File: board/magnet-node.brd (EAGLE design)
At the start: 22.8 x 23.1 mm, 28 parts, among them X1 SMA-142-0701-801/806

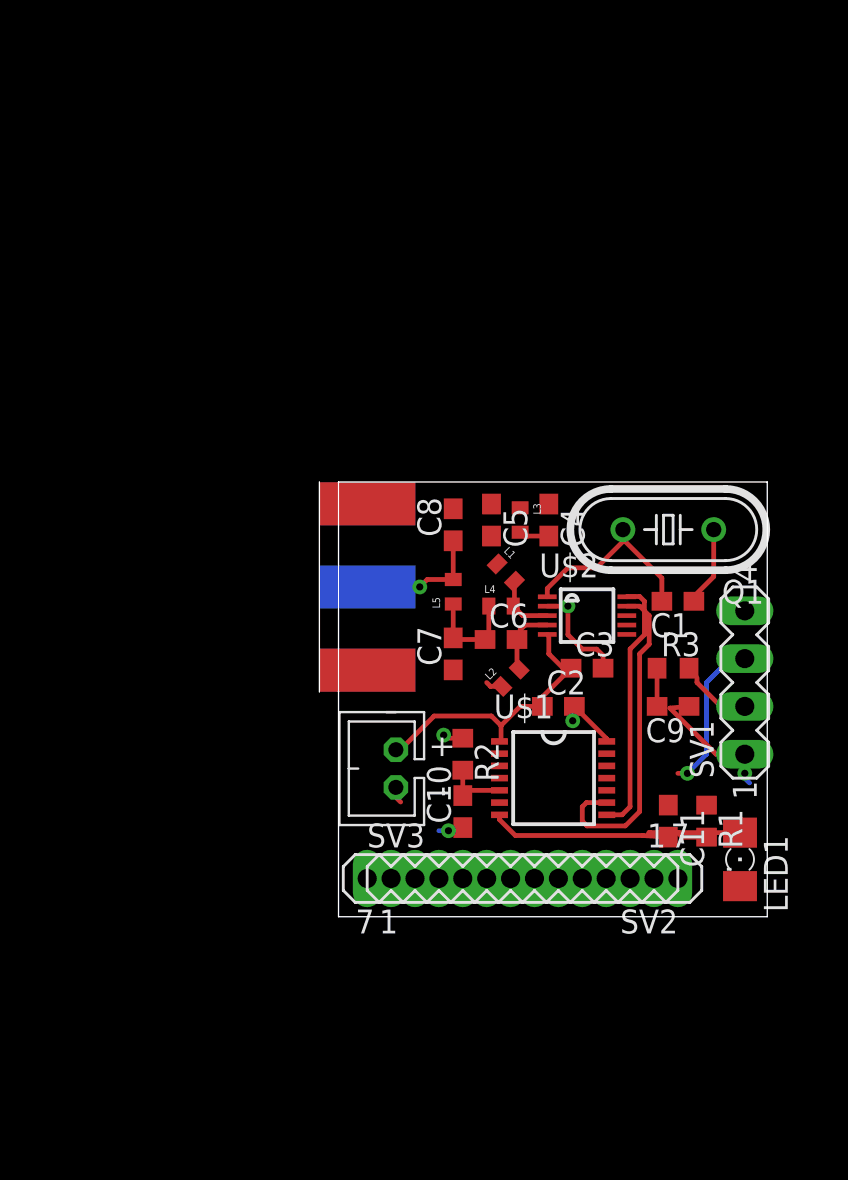
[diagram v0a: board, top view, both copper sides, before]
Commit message: initial route
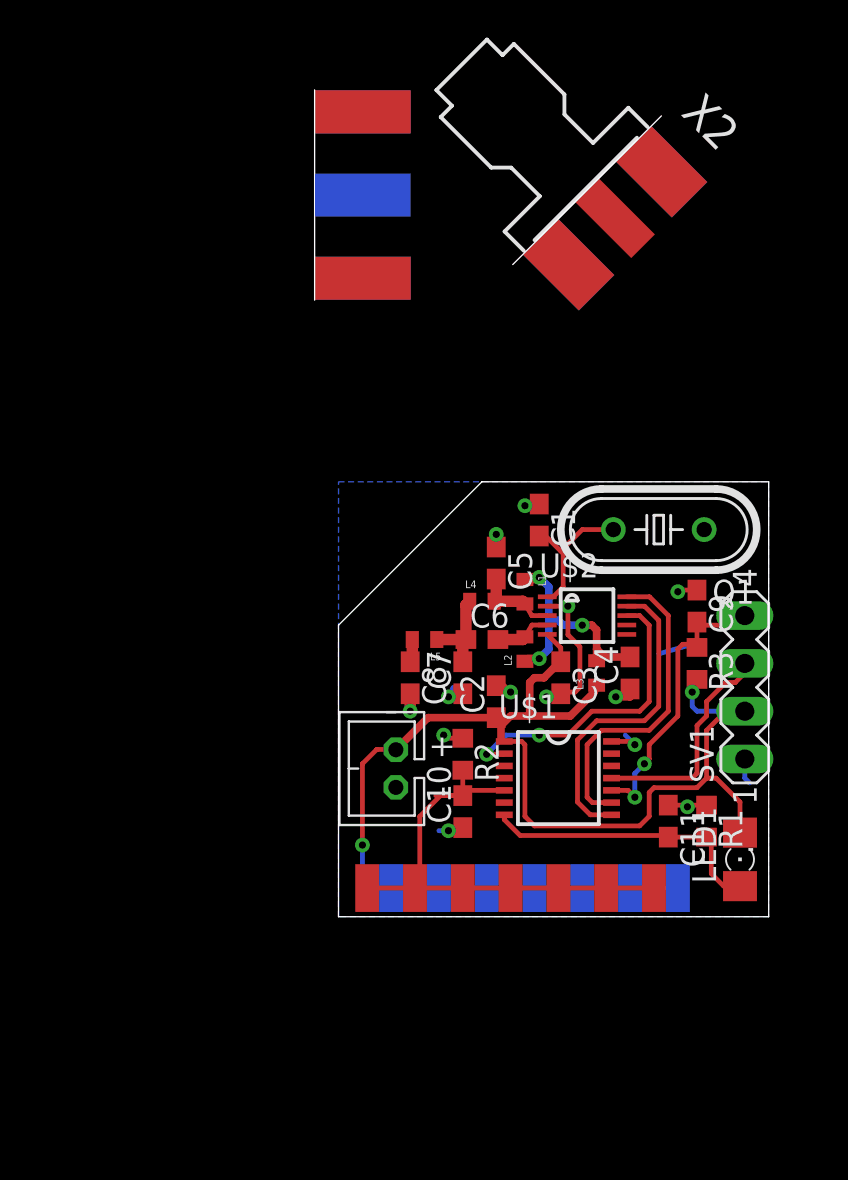
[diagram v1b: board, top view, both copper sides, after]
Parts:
- added X2: SMA-142-0711-821/826, con-coax:J502-ND-142-0711-821/826
- SV2, SV3: device con-lstb:MA07-1 -> Mine:MA07-1-SMD
- moved X1 20.8 mm to (-1.27, 42.9)
- moved C4 9.20 mm to (15.5, 17.5), turned to 90 degrees
- moved L3 9.09 mm to (13.7, 17.5), turned to 90 degrees
- moved C1 8.54 mm to (10.7, 25.7), turned to 270 degrees
- moved C8 8.44 mm to (3.81, 17.3), turned to 270 degrees
- moved C9 5.48 mm to (19.1, 21.1), turned to 270 degrees
- moved C2 3.31 mm to (8.38, 16.0), turned to 90 degrees
- moved L5 2.96 mm to (4.57, 19.3), turned to 180 degrees
- moved C5 2.30 mm to (8.38, 23.4)
- moved L2 1.70 mm to (9.91, 18.8), turned to 90 degrees
- moved C3 1.49 mm to (11.8, 17.3), turned to 270 degrees
- moved L1 1.44 mm to (9.91, 21.8), turned to 270 degrees
- moved C7 1.37 mm to (6.60, 17.3)
- moved SV2 1.37 mm to (10.4, 6.10), flipped to the bottom, turned to 0 degrees
- moved SV3 1.37 mm to (9.14, 6.10)
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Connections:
- new net N$1: U$1.2, U$2.8
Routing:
- net +3V3: track 18.6 -> 75.3 mm, vias 0 -> 2
- net N$12: track 3.41 -> 27.2 mm
- net N$1: track 0.00 -> 16.2 mm, vias 0 -> 2
- net N$15: track 2.03 -> 15.8 mm, vias 0 -> 2
- net N$4: track 2.50 -> 12.7 mm, vias 0 -> 3
- net N$10: track 6.77 -> 1.23 mm, vias 1 -> 0
- net N$3: track 13.2 -> 17.0 mm
- net N$2: track 8.31 -> 11.8 mm, vias 1 -> 0
- net N$5: track 10.3 -> 7.76 mm
- net N$13: track 17.1 -> 15.2 mm
- net N$8: track 3.36 -> 4.75 mm
- net N$6: track 18.2 -> 17.0 mm
- net N$9: track 3.75 -> 3.05 mm
- net GND: vias 5 -> 13
- added copper zone on layer 16, net GND
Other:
- board size 22.8 x 23.1 mm -> 22.9 x 23.1 mm

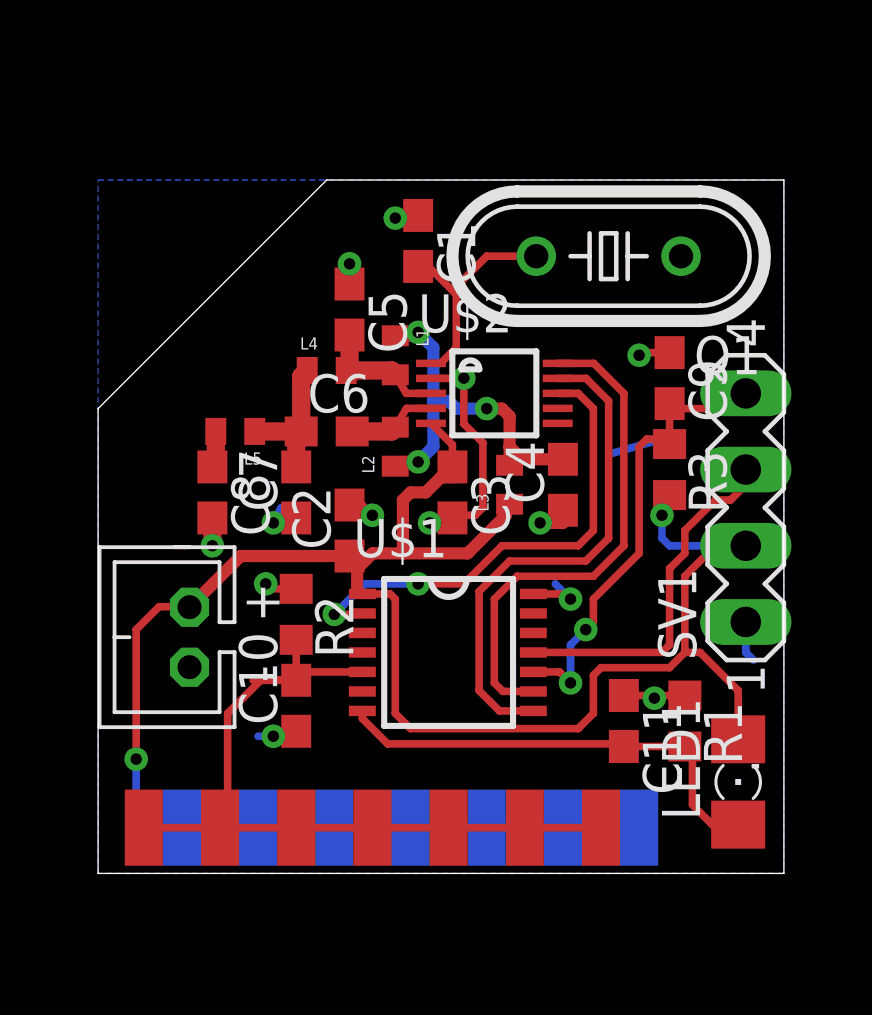
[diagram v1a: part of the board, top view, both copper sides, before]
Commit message: changing sensor power arragment
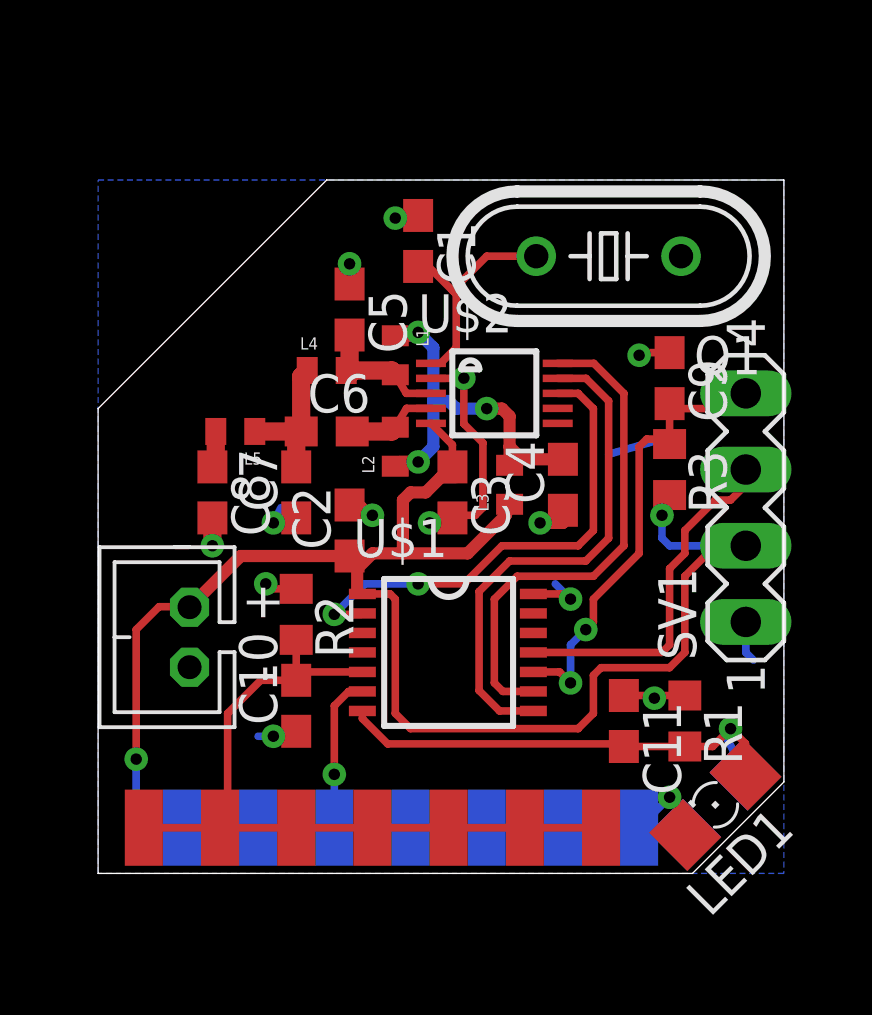
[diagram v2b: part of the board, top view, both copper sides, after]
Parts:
- added LED2: (no value), led:1206
- moved LED1 1.08 mm to (20.6, 6.86), turned to 225 degrees
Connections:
- new net VCCS: LED1.C, LED2.C, SV2.1, SV2.2, SV2.3, SV2.4, SV2.5, SV2.6, SV2.7, U$1.6
- net +3V3: no longer LED1.C, SV2.1, SV2.2, SV2.3, SV2.4, SV2.5, SV2.6, SV2.7
- net N$13: now also LED2.A
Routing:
- net VCCS: track 0.00 -> 26.1 mm, vias 0 -> 2
- net +3V3: track 75.3 -> 55.1 mm
- net N$13: track 15.2 -> 17.3 mm, vias 0 -> 1
- net N$12: track 27.2 -> 25.7 mm
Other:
- outline, holes or cut-outs redrawn
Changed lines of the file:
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@@
 <board>
 <plain>
-<wire x1="0" y1="4.572" x2="22.86" y2="4.572" width="0" layer="20"/>
+<wire x1="0" y1="4.572" x2="19.812" y2="4.572" width="0" layer="20"/>
 <dimension x1="0" y1="4.572" x2="0" y2="27.676" x3="-13.208" y3="16.124" textsize="1.778" layer="51"/>
 <dimension x1="0" y1="27.676" x2="22.784" y2="27.676" x3="11.392" y3="34.036" textsize="1.778" layer="51"/>
 <wire x1="7.62" y1="27.686" x2="0" y2="20.066" width="0" layer="20"/>
 <wire x1="7.62" y1="27.686" x2="22.86" y2="27.686" width="0" layer="20"/>
-<wire x1="22.86" y1="27.686" x2="22.86" y2="4.572" width="0" layer="20"/>
+<wire x1="22.86" y1="27.686" x2="22.86" y2="7.62" width="0" layer="20"/>
 <wire x1="0" y1="20.066" x2="0" y2="4.572" width="0" layer="20"/>
+<wire x1="19.812" y1="4.572" x2="22.86" y2="7.62" width="0" layer="20"/>
 </plain>
 <attributes>
@@
 <element name="R1" library="rcl" package="R0603" value="" x="19.558" y="9.652" rot="R270"/>
 <element name="R2" library="rcl" package="R0603" value="" x="6.604" y="13.208" rot="R270"/>
-<element name="LED1" library="led" package="1206" value="" x="21.336" y="7.62" rot="R90"/>
+<element name="LED1" library="led" package="1206" value="" x="20.574" y="6.858" rot="R225"/>
 <element name="R3" library="rcl" package="R0603" value="" x="19.05" y="18.034" rot="R270"/>
 <element name="C9" library="rcl" package="C0603" value="" x="19.05" y="21.082" rot="R270"/>
@@
 <attribute name="OC_FARNELL" value="1019328" x="13.208" y="43.18" size="1.778" layer="27" rot="R315" display="off"/>
 </element>
+<element name="LED2" library="led" package="1206" value="" x="20.574" y="6.858" rot="MR315"/>
 </elements>
 <signals>
@@
 <contactref element="J2" pad="1"/>
 <contactref element="L3" pad="1"/>
-<contactref element="LED1" pad="C"/>
-<contactref element="SV2" pad="7"/>
-<contactref element="SV2" pad="6"/>
-<contactref element="SV2" pad="5"/>
-<contactref element="SV2" pad="4"/>
-<contactref element="SV2" pad="3"/>
-<contactref element="SV2" pad="2"/>
-<contactref element="SV2" pad="1"/>
 <contactref element="R3" pad="2"/>
 <wire x1="3.048" y1="13.446" x2="3.286" y2="13.446" width="0.254" layer="1"/>
@@
 <wire x1="10.414" y1="9.398" x2="9.906" y2="9.906" width="0.254" layer="1"/>
 <wire x1="9.906" y1="9.906" x2="9.906" y2="13.716" width="0.254" layer="1"/>
-<wire x1="15.494" y1="6.096" x2="12.954" y2="6.096" width="0.254" layer="16"/>
-<wire x1="12.954" y1="6.096" x2="10.414" y2="6.096" width="0.254" layer="16"/>
-<wire x1="21.336" y1="9.042" x2="21.336" y2="10.668" width="0.254" layer="1"/>
-<wire x1="21.336" y1="10.668" x2="20.066" y2="11.938" width="0.254" layer="1"/>
-<wire x1="20.066" y1="11.938" x2="19.558" y2="11.938" width="0.254" layer="1"/>
 <wire x1="1.27" y1="12.7" x2="2.032" y2="13.462" width="0.254" layer="1"/>
 <wire x1="2.032" y1="13.462" x2="3.032" y2="13.462" width="0.254" layer="1"/>
@@
 <wire x1="11.811" y1="18.122" x2="11.811" y2="18.8579" width="0.254" layer="1"/>
 <wire x1="11.811" y1="18.8579" x2="11.0949" y2="19.574" width="0.254" layer="1"/>
-<wire x1="18.034" y1="6.096" x2="15.494" y2="6.096" width="0.254" layer="16"/>
-<wire x1="10.414" y1="6.096" x2="7.874" y2="6.096" width="0.254" layer="16"/>
-<wire x1="2.794" y1="6.096" x2="5.334" y2="6.096" width="0.254" layer="16"/>
-<wire x1="5.334" y1="6.096" x2="7.874" y2="6.096" width="0.254" layer="16"/>
 <wire x1="1.27" y1="6.604" x2="1.27" y2="8.382" width="0.254" layer="16"/>
 <via x="1.27" y="8.382" extent="1-16" drill="0.381" shape="octagon"/>
 <wire x1="1.27" y1="8.382" x2="1.27" y2="12.7" width="0.254" layer="1"/>
-<wire x1="2.794" y1="6.096" x2="1.778" y2="6.096" width="0.254" layer="16"/>
 <wire x1="1.778" y1="6.096" x2="1.27" y2="6.604" width="0.254" layer="16"/>
 </signal>
@@
 <wire x1="6.882" y1="11.288" x2="6.604" y2="11.01" width="0.254" layer="1"/>
 <wire x1="6.604" y1="12.358" x2="6.604" y2="11.01" width="0.254" layer="1"/>
-<wire x1="6.604" y1="11.01" x2="5.168" y2="11.01" width="0.254" layer="1"/>
 <wire x1="1.524" y1="6.096" x2="4.064" y2="6.096" width="0.254" layer="1"/>
 <wire x1="4.064" y1="6.096" x2="6.604" y2="6.096" width="0.254" layer="1"/>
@@
 <wire x1="17.438" y1="8.89" x2="17.526" y2="8.802" width="0.254" layer="1"/>
 <wire x1="17.526" y1="8.802" x2="19.558" y2="8.802" width="0.254" layer="1"/>
-<wire x1="21.336" y1="6.198" x2="20.472" y2="6.198" width="0.254" layer="1"/>
-<wire x1="20.472" y1="6.198" x2="19.812" y2="6.858" width="0.254" layer="1"/>
-<wire x1="19.812" y1="6.858" x2="19.812" y2="8.548" width="0.254" layer="1"/>
-<wire x1="19.812" y1="8.548" x2="19.558" y2="8.802" width="0.254" layer="1"/>
+<contactref element="LED2" pad="A"/>
+<wire x1="21.579503125" y1="7.863503125" x2="21.322" y2="8.534" width="0.254" layer="1"/>
+<wire x1="21.57950625" y1="7.863503125" x2="20.98" y2="9.042" width="0.254" layer="16"/>
+<wire x1="20.98" y1="9.042" x2="21.082" y2="9.398" width="0.254" layer="16"/>
+<via x="21.082" y="9.398" extent="1-16" drill="0.381" shape="octagon"/>
+<wire x1="19.558" y1="8.802" x2="20.486" y2="8.802" width="0.254" layer="1"/>
+<wire x1="20.486" y1="8.802" x2="21.082" y2="9.398" width="0.254" layer="1"/>
+<wire x1="21.579503125" y1="7.863503125" x2="21.579503125" y2="8.900496875" width="0.254" layer="1"/>
+<wire x1="21.579503125" y1="8.900496875" x2="21.082" y2="9.398" width="0.254" layer="1"/>
 </signal>
 <signal name="N$15">
@@
 <wire x1="8.779" y1="13.208" x2="8.809" y2="13.238" width="0.254" layer="1"/>
 </signal>
+<signal name="VCCS">
+<contactref element="SV2" pad="7"/>
+<contactref element="SV2" pad="6"/>
+<contactref element="SV2" pad="5"/>
+<contactref element="SV2" pad="4"/>
+<contactref element="SV2" pad="3"/>
+<contactref element="SV2" pad="2"/>
+<contactref element="SV2" pad="1"/>
+<wire x1="15.494" y1="6.096" x2="12.954" y2="6.096" width="0.254" layer="16"/>
+<wire x1="12.954" y1="6.096" x2="10.414" y2="6.096" width="0.254" layer="16"/>
+<wire x1="18.034" y1="6.096" x2="15.494" y2="6.096" width="0.254" layer="16"/>
+<wire x1="10.414" y1="6.096" x2="7.874" y2="6.096" width="0.254" layer="16"/>
+<wire x1="2.794" y1="6.096" x2="5.334" y2="6.096" width="0.254" layer="16"/>
+<wire x1="5.334" y1="6.096" x2="7.874" y2="6.096" width="0.254" layer="16"/>
+<contactref element="LED1" pad="C"/>
+<contactref element="LED2" pad="C"/>
+<contactref element="U$1" pad="6"/>
+<wire x1="8.809" y1="10.638" x2="8.352" y2="10.638" width="0.254" layer="1"/>
+<wire x1="8.352" y1="10.638" x2="7.874" y2="10.16" width="0.254" layer="1"/>
+<wire x1="7.874" y1="10.16" x2="7.874" y2="7.874" width="0.254" layer="1"/>
+<via x="7.874" y="7.874" extent="1-16" drill="0.381" shape="octagon"/>
+<wire x1="7.874" y1="7.874" x2="7.874" y2="6.096" width="0.254" layer="16"/>
+<wire x1="19.56849375" y1="5.85249375" x2="20.168" y2="6.198" width="0.254" layer="1"/>
+<wire x1="20.168" y1="6.198" x2="19.05" y2="7.112" width="0.254" layer="1"/>
+<via x="19.05" y="7.112" extent="1-16" drill="0.381" shape="octagon"/>
+<wire x1="19.05" y1="7.112" x2="18.034" y2="6.096" width="0.254" layer="16"/>
+<wire x1="19.568496875" y1="5.85249375" x2="20.168" y2="6.198" width="0.254" layer="16"/>
+<wire x1="20.168" y1="6.198" x2="19.05" y2="7.112" width="0.254" layer="16"/>
+</signal>
 </signals>
